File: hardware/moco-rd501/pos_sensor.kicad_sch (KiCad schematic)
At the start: 4 parts, among them U5 AS5147

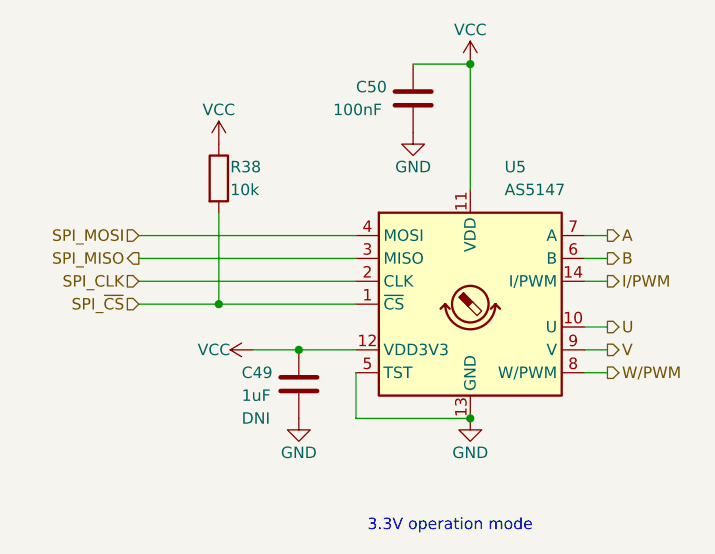
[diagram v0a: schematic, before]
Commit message: Rename "moco-s" to "moco-rd501"
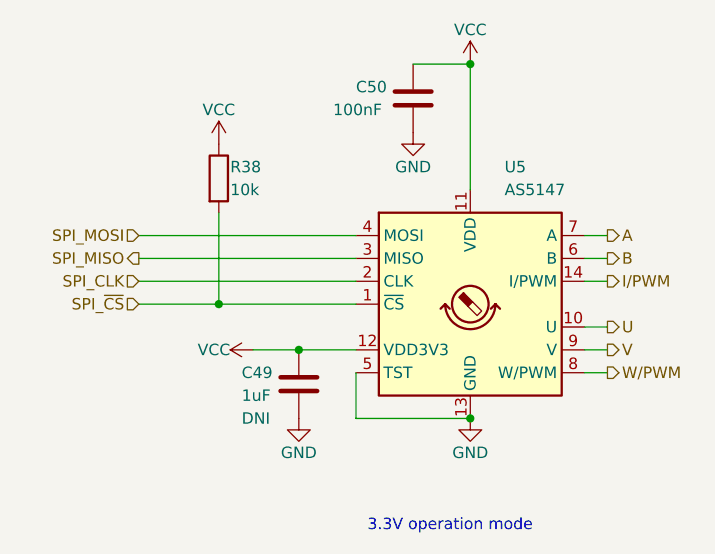
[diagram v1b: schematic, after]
